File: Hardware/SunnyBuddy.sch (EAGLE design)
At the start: 38 parts, among them J1 5.5x2.1mm Barrel, J2 POWER_JACKPTH, J5 M02PTH, J6 M023.5MM, J7 M023.5MM, J8 M023.5MM, U1 LT3652

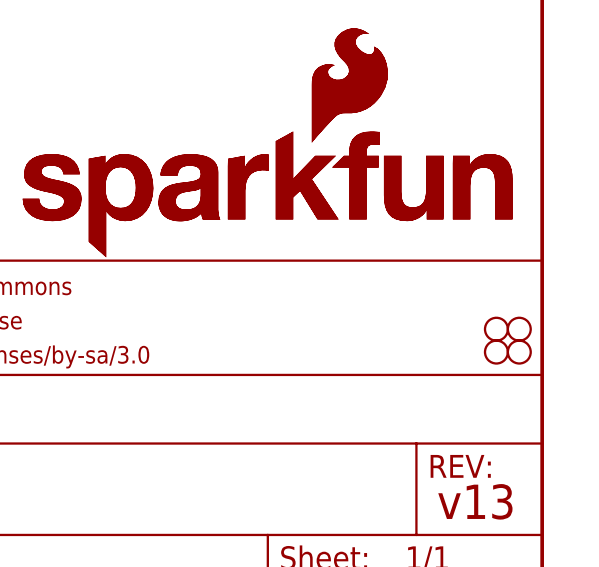
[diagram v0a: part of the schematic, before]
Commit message: added board fiducials
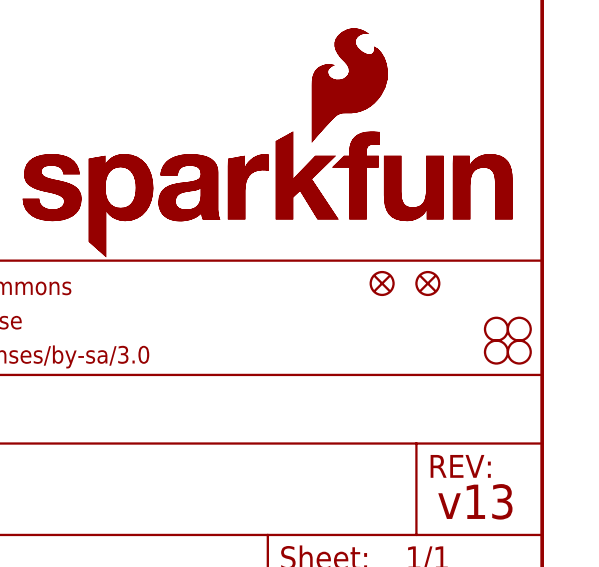
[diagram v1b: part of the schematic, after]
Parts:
- added FID1, FID2: FIDUCIAL1X2, SparkFun-Aesthetics:FIDUCIAL1X2
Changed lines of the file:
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@@
 <?xml version="1.0" encoding="utf-8"?>
 <!DOCTYPE eagle SYSTEM "eagle.dtd">
-<eagle version="6.5.0">
+<eagle version="6.6.0">
 <drawing>
 <settings>
@@
 <part name="LOGO3" library="SparkFun-Aesthetics" deviceset="OSHW-LOGO" device="S"/>
 <part name="LOGO4" library="SparkFun-Aesthetics" deviceset="SFE_LOGO_NAME_FLAME" device=".3_INCH"/>
+<part name="FID1" library="SparkFun-Aesthetics" deviceset="FIDUCIAL" device="1X2"/>
+<part name="FID2" library="SparkFun-Aesthetics" deviceset="FIDUCIAL" device="1X2"/>
 </parts>
 <sheets>
@@
 <instance part="LOGO3" gate="G$1" x="175.26" y="48.26"/>
 <instance part="LOGO4" gate="G$1" x="190.5" y="35.56"/>
+<instance part="FID1" gate="G$1" x="231.14" y="33.02"/>
+<instance part="FID2" gate="G$1" x="236.22" y="33.02"/>
 </instances>
 <busses>
